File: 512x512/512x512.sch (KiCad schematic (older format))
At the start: 28 parts, among them J1 CONN_01X39, U1 SST39SF040, U2 AS6C4008-55PCN, U3 74LS670, U4 74LS670, U5 74LS139, U6 74LS74, U7 74LS138

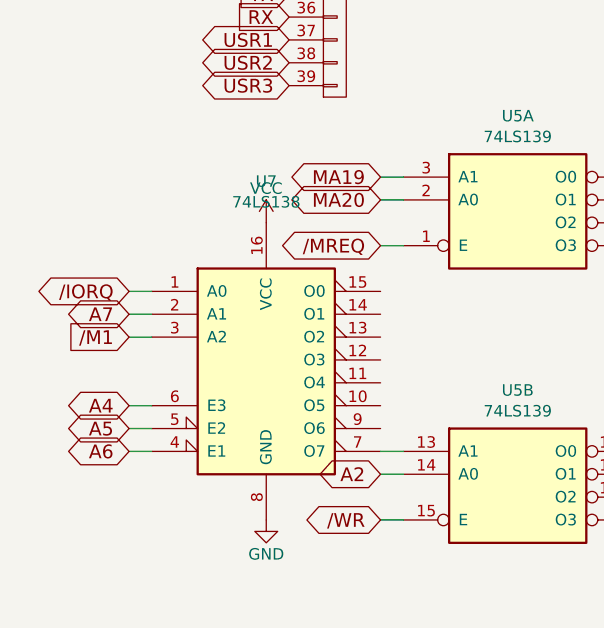
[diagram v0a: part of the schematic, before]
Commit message: Fixing schematic errors. With these fixes, the thing actually boots.
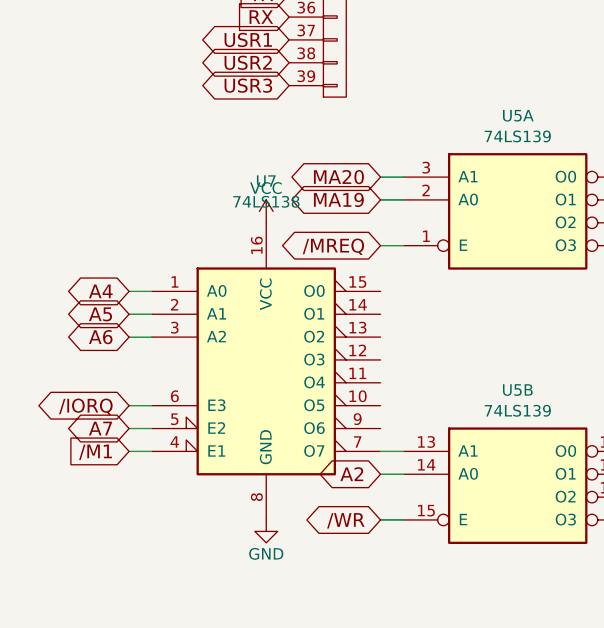
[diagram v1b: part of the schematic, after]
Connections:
- net /IORQ: now also U7.6 (E3); no longer U7.1 (A0)
- net /M1: now also U7.4 (E1); no longer U7.3 (A2)
- net A4: now also U7.1 (A0); no longer U7.6 (E3)
- net A5: now also U7.2 (A1); no longer U7.5 (E2)
- net A6: now also U7.3 (A2); no longer U7.4 (E1)
- net A7: now also U7.5 (E2); no longer U7.2 (A1)
- net MA19: now also U5.2 (A0); no longer U5.3 (A1)
- net MA20: now also U5.3 (A1); no longer U5.2 (A0)
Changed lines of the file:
@@
 	1    0    0    -1
 $EndComp
-Text GLabel 900  6200 0    60   3State ~ 0
+Text GLabel 900  6700 0    60   3State ~ 0
 /IORQ
-Text GLabel 900  6300 0    60   3State ~ 0
+Text GLabel 900  6800 0    60   3State ~ 0
 A7
-Text GLabel 900  6400 0    60   Input ~ 0
+Text GLabel 900  6900 0    60   Input ~ 0
 /M1
 Wire Wire Line
@@
 Wire Wire Line
 	900  6200 1000 6200
-Text GLabel 900  6900 0    60   3State ~ 0
-A6
-Text GLabel 900  6800 0    60   3State ~ 0
-A5
-Text GLabel 900  6700 0    60   3State ~ 0
-A4
 Wire Wire Line
 	1000 6800 900  6800
@@
 Wire Wire Line
 	2000 6000 2100 6000
+Text GLabel 2000 5800 0    60   BiDi ~ 0
+MA19
+Wire Wire Line
+	2000 5700 2100 5700
 Text GLabel 2000 5700 0    60   BiDi ~ 0
-MA19
-Wire Wire Line
-	2000 5700 2100 5700
-Text GLabel 2000 5800 0    60   BiDi ~ 0
 MA20
 Wire Wire Line
@@
 Wire Wire Line
 	8800 7050 9300 7050
+Text GLabel 900  6300 0    60   3State ~ 0
+A5
+Text GLabel 900  6400 0    60   3State ~ 0
+A6
+Text GLabel 900  6200 0    60   3State ~ 0
+A4
 $EndSCHEMATC

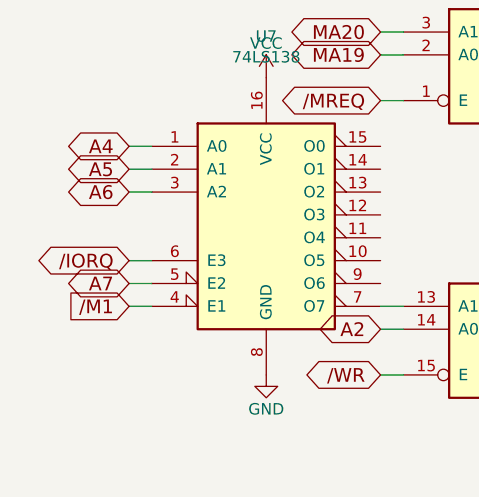
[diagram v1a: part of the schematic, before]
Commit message: Even with the most recent updates, ~M1 and IOREQ were crossed. Fixed on PCBs here, fixed with wire on the boards I have.
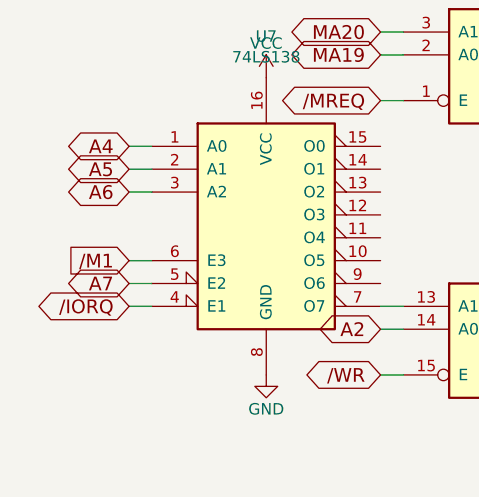
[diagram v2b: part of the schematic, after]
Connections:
- net /IORQ: now also U7.4 (E1); no longer U7.6 (E3)
- net /M1: now also U7.6 (E3); no longer U7.4 (E1)
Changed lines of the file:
@@
 	1    0    0    -1
 $EndComp
-Text GLabel 900  6700 0    60   3State ~ 0
+Text GLabel 900  6900 0    60   3State ~ 0
 /IORQ
 Text GLabel 900  6800 0    60   3State ~ 0
 A7
-Text GLabel 900  6900 0    60   Input ~ 0
+Text GLabel 900  6700 0    60   Input ~ 0
 /M1
 Wire Wire Line
